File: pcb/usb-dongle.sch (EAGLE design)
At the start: 40 parts, among them IC1 STM32F103C8, IC2 TPS76333, IC3 NRF24L01-MOD-SMD, Q1 8MHz, SW1 KSS-2EG4430, X1 USB-MALE-A-H

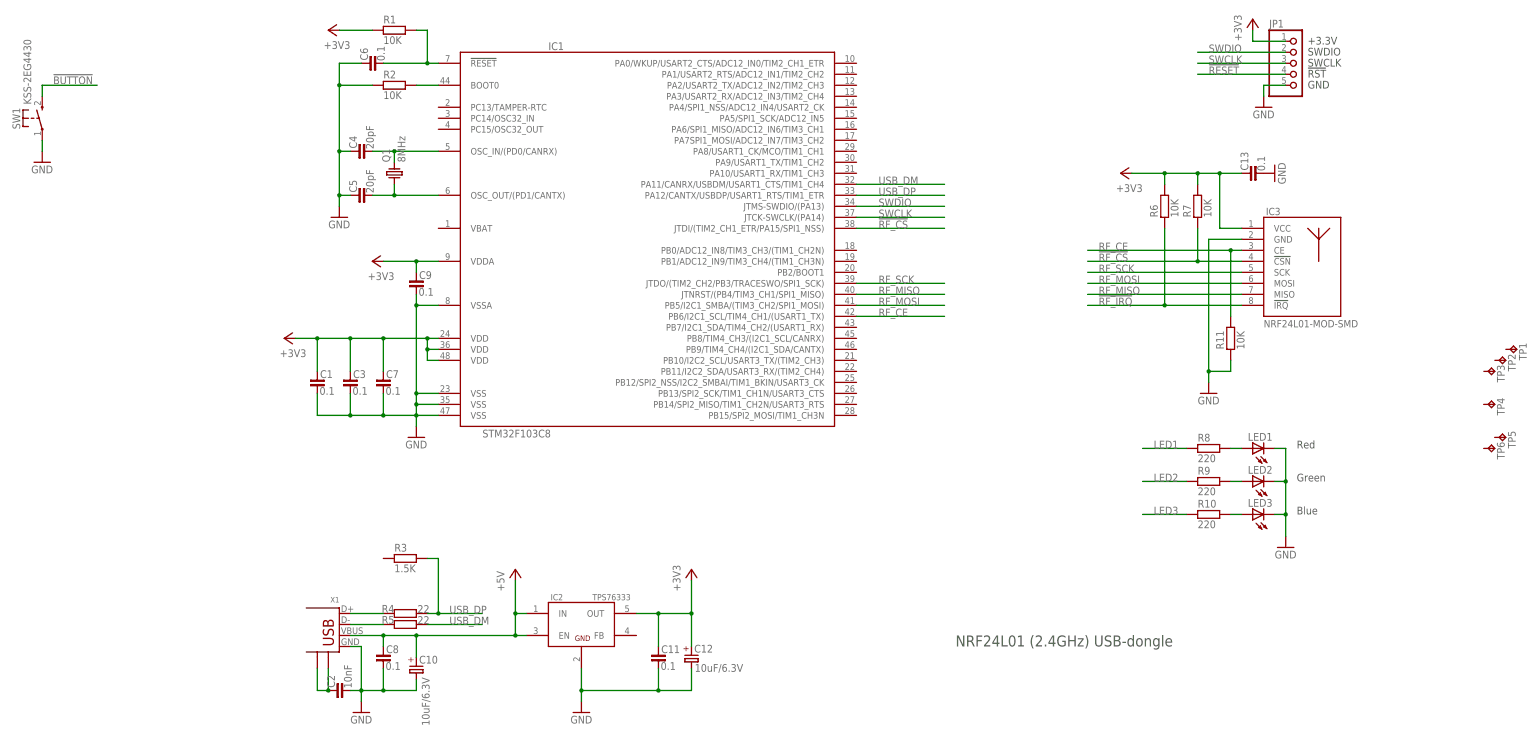
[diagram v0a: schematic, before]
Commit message: USB-dongle. need review
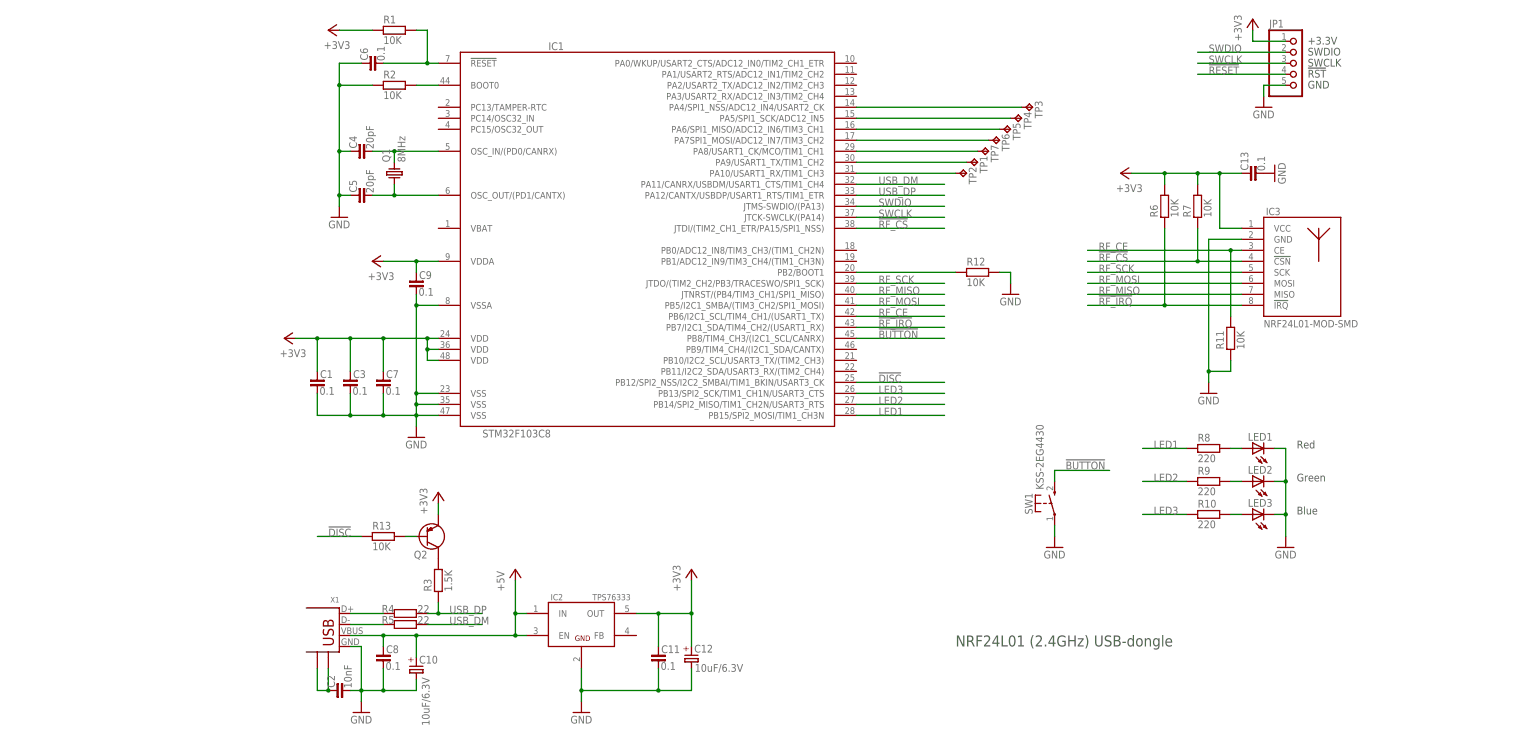
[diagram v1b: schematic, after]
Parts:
- added Q2: (no value), semiconductor:PNP-SOT23
- added R12, R13: 10K, rc-master-smd:R_0603
- added TP7: TPB1,27, testpad:TPB1,27
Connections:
- new net !DISC: IC1.PB12/SPI2_NSS/I2C2_SMBAI/TIM1_BKIN/USART3_CK, R13.1
- new net N$12: IC1.PA4/SPI1_NSS/ADC12_IN4/USART2_CK, TP3.TP
- new net N$13: IC1.PA5/SPI1_SCK/ADC12_IN5, TP4.TP
- new net N$14: IC1.PA6/SPI1_MISO/ADC12_IN6/TIM3_CH1, TP5.TP
- new net N$15: IC1.PA7SPI1_MOSI/ADC12_IN7/TIM3_CH2, TP6.TP
- new net N$16: IC1.PA8/USART1_CK/MCO/TIM1_CH1, TP7.TP
- new net N$17: IC1.PB2/BOOT1, R12.1
- new net N$18: Q2.B, R13.2
- new net N$19: Q2.C, R3.2
- new net N$4: IC1.PA9/USART1_TX/TIM1_CH2, TP1.TP
- new net N$5: IC1.PA10/USART1_RX/TIM1_CH3, TP2.TP
- net !BUTTON: now also IC1.PB8/TIM4_CH3/(I2C1_SCL/CANRX)
- net !RF_IRQ: now also IC1.PB7/I2C1_SDA/TIM4_CH2/(USART1_RX)
- net +3V3: now also Q2.E
- net GND: now also R12.2
- net LED1: now also IC1.PB15/SPI2_MOSI/TIM1_CH3N
- net LED2: now also IC1.PB14/SPI2_MISO/TIM1_CH2N/USART3_RTS
- net LED3: now also IC1.PB13/SPI2_SCK/TIM1_CH1N/USART3_CTS
- net USB_DP: now also R3.1; no longer R3.2
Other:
- moved on the sheet: R3, SW1, TP1, TP2, TP3, TP4, TP5, TP6
